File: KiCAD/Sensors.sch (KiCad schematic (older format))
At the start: 29 parts, among them U401 BME680, U402 APDS-9500, U403 LSM6DSM, U404 CMM-4030D-261-I2S-TR, U405 TSOP75340TTCT-ND, U406 MAX86150EFF+T, U407 VL6180XV0NR_1, U408 LP5907MFX-2.8

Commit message: Continue work on Schematics
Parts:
- removed U408: LP5907MFX-2.8, Package_TO_SOT_SMD:SOT-23-5, symbol Regulator_Linear:LP5907MFX-2.8
- added PW501: AP7354-18FS4, XasPrints:X2-DFN1010-4, symbol XasParts:AP7354-18FS4
- added PW502: AP7354-28FS4, XasPrints:X2-DFN1010-4, symbol XasParts:AP7354-28FS4
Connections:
- net labels removed: +1V8
- wire segments 125 -> 130
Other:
- moved on the sheet: C407, C408, C409, C410, C411, D408, R402, U403, U406

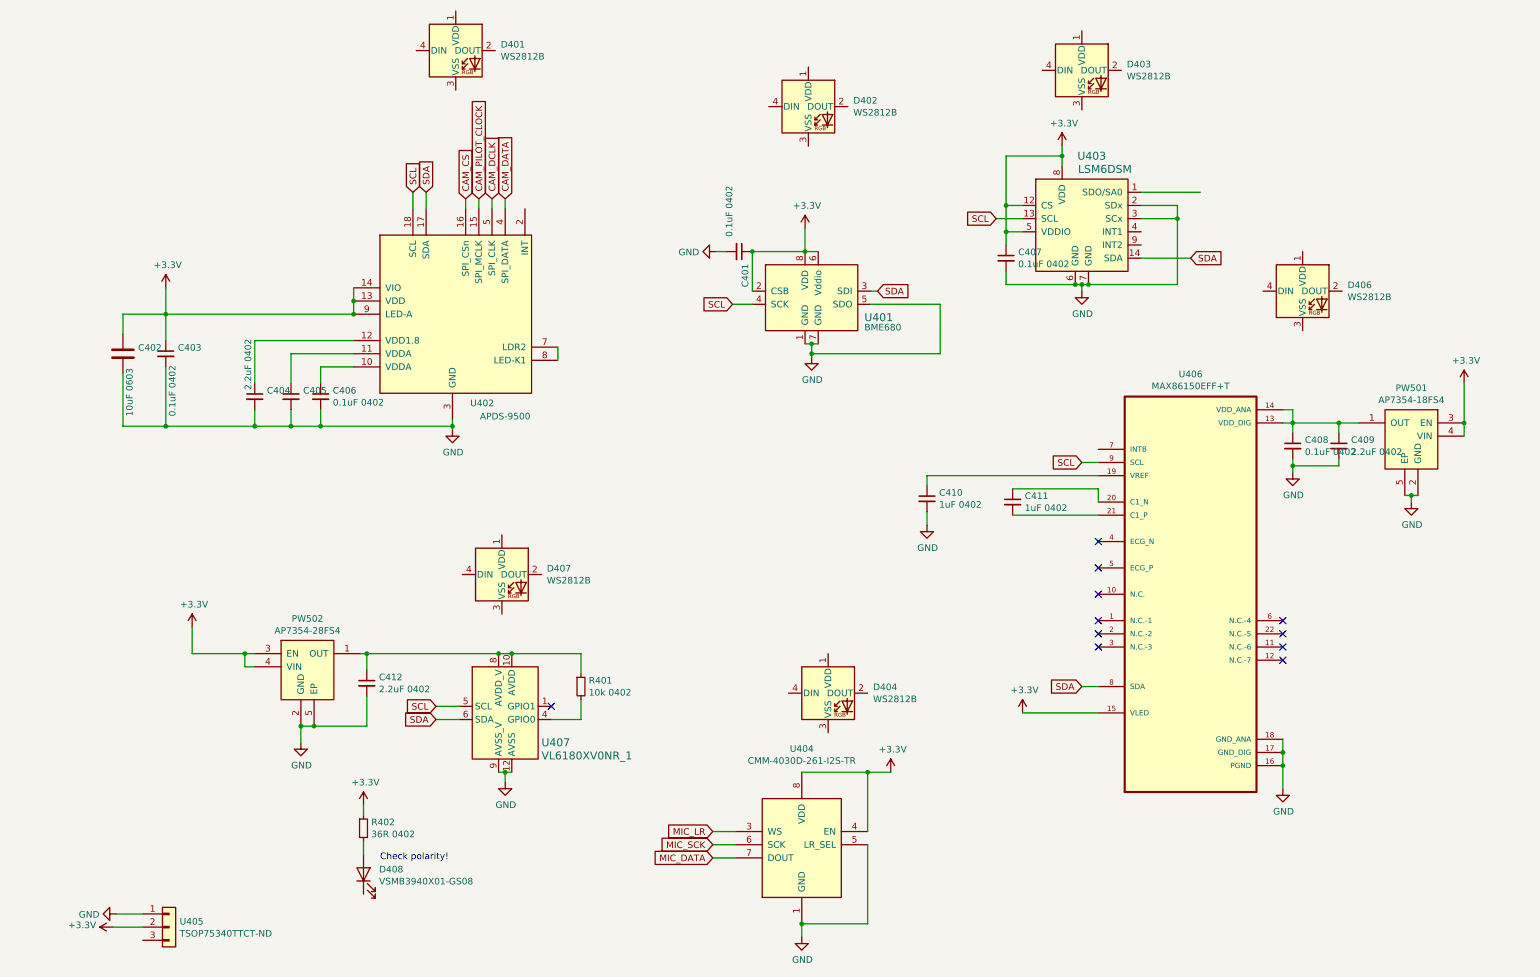
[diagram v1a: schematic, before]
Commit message: Add STM32 base circuit for power control and USB, also a lot of other things
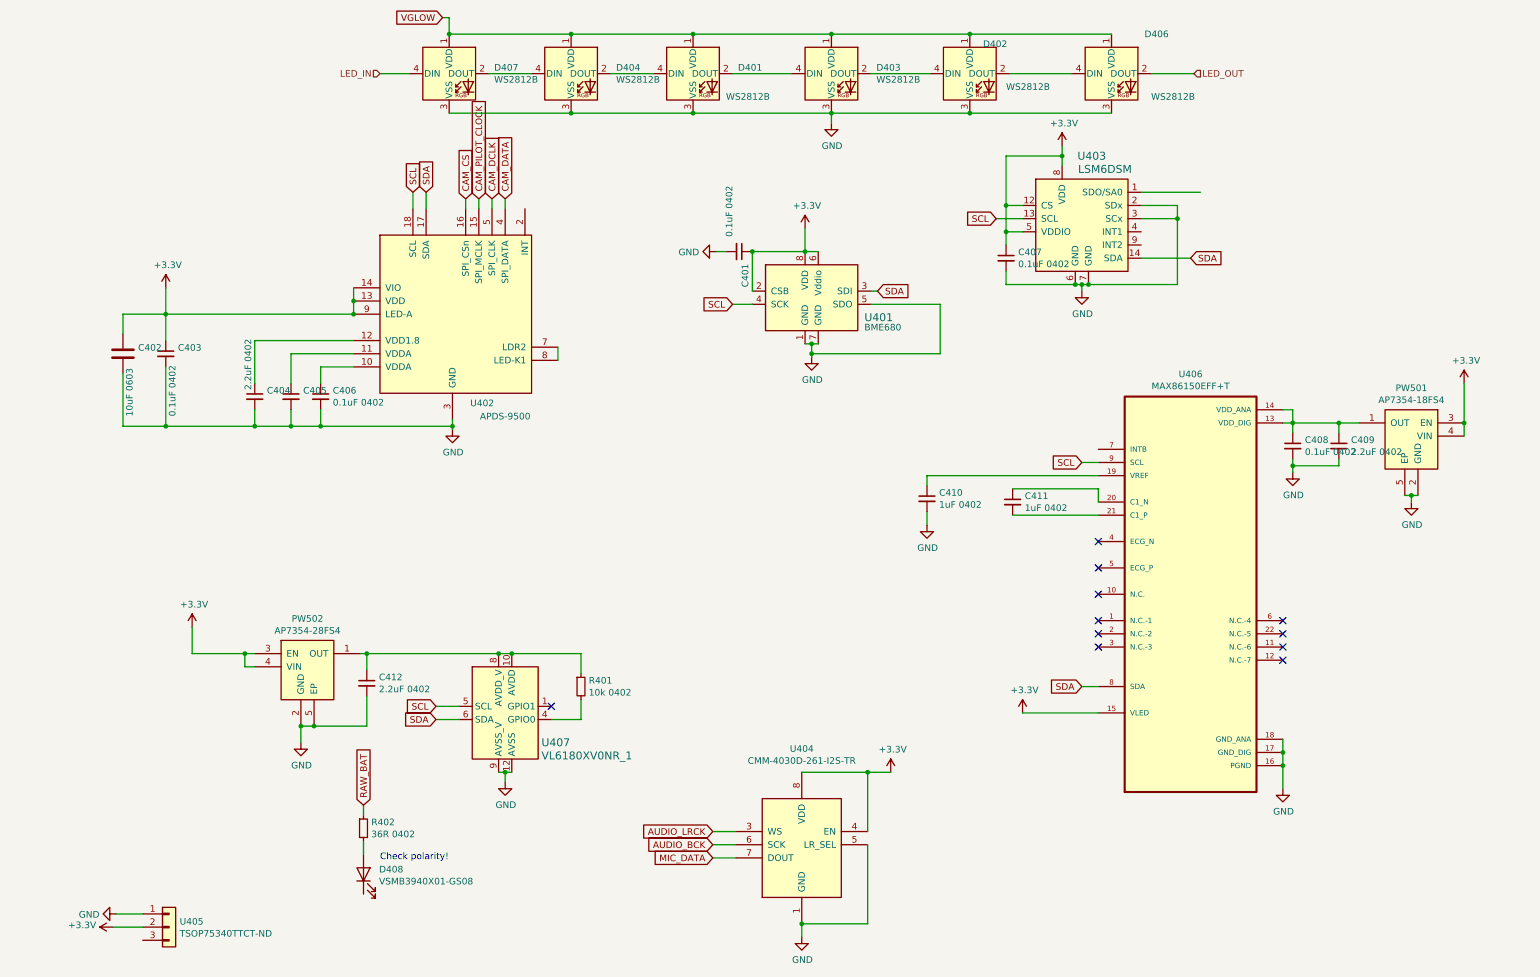
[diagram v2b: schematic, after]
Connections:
- net +3V3: no longer R402.1
- net GND: now also D401.3 (VSS), D402.3 (VSS), D403.3 (VSS), D404.3 (VSS), D406.3 (VSS), D407.3 (VSS)
- net VGLOW: now reaches D401.1 (VDD)
- net VGLOW: now also D402.1 (VDD), D403.1 (VDD), D404.1 (VDD), D406.1 (VDD), D407.1 (VDD)
- net at D401.2 (DOUT): now also D403.4 (DIN)
- net at D401.4 (DIN): now also D404.2 (DOUT)
- net at D402.2 (DOUT): now also D406.4 (DIN)
- net at D402.4 (DIN): now also D403.2 (DOUT)
- net at D404.4 (DIN): now also D407.2 (DOUT)
- net LED_OUT: now reaches D406.2 (DOUT)
- net LED_IN: now reaches D407.4 (DIN)
- net MIC_LR renamed AUDIO_LRCK
- net MIC_SCK renamed AUDIO_BCK
- new net RAW_BAT: R402.1
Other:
- moved on the sheet: D401, D402, D403, D404, D406, D407
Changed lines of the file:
@@
 $Descr A4 11693 8268
 encoding utf-8
-Sheet 5 7
+Sheet 4 6
 Title ""
 Date ""
@@
 L LED:WS2812B D401
 U 1 1 60F3BC6A
-P 3500 850
-F 0 "D401" H 3841 896 50  0000 L CNN
-F 1 "WS2812B" H 3841 805 50  0000 L CNN
-F 2 "XasPrints:SMD-LX0707RGB-TR" H 3550 550 50  0001 L TNN
-F 3 "https://cdn-shop.adafruit.com/datasheets/WS2812B.pdf" H 3600 475 50  0001 L TNN
-	1    3500 850
+P 5300 1025
+F 0 "D401" H 5641 1071 50  0000 L CNN
+F 1 "WS2812B" H 5550 850 50  0000 L CNN
+F 2 "XasPrints:SMD-LX0707RGB-TR" H 5350 725 50  0001 L TNN
+F 3 "https://cdn-shop.adafruit.com/datasheets/WS2812B.pdf" H 5400 650 50  0001 L TNN
+	1    5300 1025
 	1    0    0    -1
 $EndComp
@@
 L LED:WS2812B D402
 U 1 1 60F4C75F
-P 6175 1275
-F 0 "D402" H 6516 1321 50  0000 L CNN
-F 1 "WS2812B" H 6516 1230 50  0000 L CNN
-F 2 "XasPrints:SMD-LX0707RGB-TR" H 6225 975 50  0001 L TNN
-F 3 "https://cdn-shop.adafruit.com/datasheets/WS2812B.pdf" H 6275 900 50  0001 L TNN
-	1    6175 1275
+P 7400 1025
+F 0 "D402" H 7500 1250 50  0000 L CNN
+F 1 "WS2812B" H 7675 925 50  0000 L CNN
+F 2 "XasPrints:SMD-LX0707RGB-TR" H 7450 725 50  0001 L TNN
+F 3 "https://cdn-shop.adafruit.com/datasheets/WS2812B.pdf" H 7500 650 50  0001 L TNN
+	1    7400 1025
 	1    0    0    -1
 $EndComp
@@
 L LED:WS2812B D403
 U 1 1 60F50157
-P 8250 1000
-F 0 "D403" H 8591 1046 50  0000 L CNN
-F 1 "WS2812B" H 8591 955 50  0000 L CNN
-F 2 "XasPrints:SMD-LX0707RGB-TR" H 8300 700 50  0001 L TNN
-F 3 "https://cdn-shop.adafruit.com/datasheets/WS2812B.pdf" H 8350 625 50  0001 L TNN
-	1    8250 1000
+P 6350 1025
+F 0 "D403" H 6691 1071 50  0000 L CNN
+F 1 "WS2812B" H 6691 980 50  0000 L CNN
+F 2 "XasPrints:SMD-LX0707RGB-TR" H 6400 725 50  0001 L TNN
+F 3 "https://cdn-shop.adafruit.com/datasheets/WS2812B.pdf" H 6450 650 50  0001 L TNN
+	1    6350 1025
 	1    0    0    -1
 $EndComp
@@
 L LED:WS2812B D404
 U 1 1 60F5023D
-P 6325 5725
-F 0 "D404" H 6666 5771 50  0000 L CNN
-F 1 "WS2812B" H 6666 5680 50  0000 L CNN
-F 2 "XasPrints:SMD-LX0707RGB-TR" H 6375 5425 50  0001 L TNN
-F 3 "https://cdn-shop.adafruit.com/datasheets/WS2812B.pdf" H 6425 5350 50  0001 L TNN
-	1    6325 5725
+P 4375 1025
+F 0 "D404" H 4716 1071 50  0000 L CNN
+F 1 "WS2812B" H 4716 980 50  0000 L CNN
+F 2 "XasPrints:SMD-LX0707RGB-TR" H 4425 725 50  0001 L TNN
+F 3 "https://cdn-shop.adafruit.com/datasheets/WS2812B.pdf" H 4475 650 50  0001 L TNN
+	1    4375 1025
 	1    0    0    -1
 $EndComp
@@
 L LED:WS2812B D406
 U 1 1 60F5FA46
-P 9925 2675
-F 0 "D406" H 10266 2721 50  0000 L CNN
-F 1 "WS2812B" H 10266 2630 50  0000 L CNN
-F 2 "XasPrints:SMD-LX0707RGB-TR" H 9975 2375 50  0001 L TNN
-F 3 "https://cdn-shop.adafruit.com/datasheets/WS2812B.pdf" H 10025 2300 50  0001 L TNN
-	1    9925 2675
+P 8475 1025
+F 0 "D406" H 8725 1325 50  0000 L CNN
+F 1 "WS2812B" H 8775 850 50  0000 L CNN
+F 2 "XasPrints:SMD-LX0707RGB-TR" H 8525 725 50  0001 L TNN
+F 3 "https://cdn-shop.adafruit.com/datasheets/WS2812B.pdf" H 8575 650 50  0001 L TNN
+	1    8475 1025
 	1    0    0    -1
 $EndComp
@@
 L LED:WS2812B D407
 U 1 1 60F5FD07
-P 3850 4825
-F 0 "D407" H 4191 4871 50  0000 L CNN
-F 1 "WS2812B" H 4191 4780 50  0000 L CNN
-F 2 "XasPrints:SMD-LX0707RGB-TR" H 3900 4525 50  0001 L TNN
-F 3 "https://cdn-shop.adafruit.com/datasheets/WS2812B.pdf" H 3950 4450 50  0001 L TNN
-	1    3850 4825
+P 3450 1025
+F 0 "D407" H 3791 1071 50  0000 L CNN
+F 1 "WS2812B" H 3791 980 50  0000 L CNN
+F 2 "XasPrints:SMD-LX0707RGB-TR" H 3500 725 50  0001 L TNN
+F 3 "https://cdn-shop.adafruit.com/datasheets/WS2812B.pdf" H 3550 650 50  0001 L TNN
+	1    3450 1025
 	1    0    0    -1
 $EndComp
@@
 Connection ~ 6125 7475
 Text GLabel 5450 6775 0    50   Input ~ 0
-MIC_LR
+AUDIO_LRCK
 Text GLabel 5450 6875 0    50   Input ~ 0
-MIC_SCK
+AUDIO_BCK
 Text GLabel 5450 6975 0    50   Input ~ 0
 MIC_DATA
@@
 Wire Wire Line
 	2800 6850 2800 6950
-$Comp
-L power:+3.3V #PWR0134
-U 1 1 6105D69A
-P 2800 6575
-F 0 "#PWR0134" H 2800 6425 50  0001 C CNN
-F 1 "+3.3V" H 2815 6748 50  0000 C CNN
-F 2 "" H 2800 6575 50  0001 C CNN
-F 3 "" H 2800 6575 50  0001 C CNN
-	1    2800 6575
-	1    0    0    -1
-$EndComp
 Wire Wire Line
 	2800 6575 2800 6650
@@
 	1    0    0    -1
 $EndComp
+Wire Wire Line
+	3750 1025 4075 1025
+Wire Wire Line
+	4675 1025 5000 1025
+Wire Wire Line
+	5600 1025 6050 1025
+Wire Wire Line
+	6650 1025 7100 1025
+Wire Wire Line
+	7700 1025 8175 1025
+Wire Wire Line
+	3450 725  4375 725
+Connection ~ 4375 725
+Wire Wire Line
+	4375 725  5300 725
+Connection ~ 5300 725
+Wire Wire Line
+	5300 725  6350 725
+Connection ~ 6350 725
+Wire Wire Line
+	6350 725  7400 725
+Connection ~ 7400 725
+Wire Wire Line
+	7400 725  8475 725
+Wire Wire Line
+	8475 1325 7400 1325
+Connection ~ 4375 1325
+Wire Wire Line
+	4375 1325 3450 1325
+Connection ~ 5300 1325
+Wire Wire Line
+	5300 1325 4375 1325
+Connection ~ 6350 1325
+Wire Wire Line
+	6350 1325 5300 1325
+Connection ~ 7400 1325
+Wire Wire Line
+	7400 1325 6350 1325
+$Comp
+L power:GND #PWR0145
+U 1 1 6110EA34
+P 6350 1400
+F 0 "#PWR0145" H 6350 1150 50  0001 C CNN
+F 1 "GND" H 6355 1227 50  0000 C CNN
+F 2 "" H 6350 1400 50  0001 C CNN
+F 3 "" H 6350 1400 50  0001 C CNN
+	1    6350 1400
+	1    0    0    -1
+$EndComp
+Wire Wire Line
+	6350 1400 6350 1325
+Text GLabel 3400 600  0    50   Input ~ 0
+VGLOW
+Wire Wire Line
+	3400 600  3450 600
+Wire Wire Line
+	3450 600  3450 725
+Connection ~ 3450 725
+Text HLabel 2925 1025 0    50   Input ~ 0
+LED_IN
+Wire Wire Line
+	2925 1025 3150 1025
+Text GLabel 2800 6575 1    50   Input ~ 0
+RAW_BAT
+Text HLabel 9100 1025 2    50   Input ~ 0
+LED_OUT
+Wire Wire Line
+	9100 1025 8775 1025
 $EndSCHEMATC

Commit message: Continue work on TapV2's schematic, almost completing it!
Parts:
- added Q401: DMN3404L, Package_TO_SOT_SMD:SOT-23, symbol Transistor_FET:DMN3404L
- added R403: 36R 0402, Resistor_SMD:R_0402_1005Metric, symbol Device:R_Small
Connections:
- net GND: now also Q401.2 (S)
- net IR_RX: now reaches U405.3 (Pin_3)
- net at D408.1 (K): now also Q401.3 (D)
- new net: Q401.1 (G), R403.1
- new net IR_TX: R403.2
- no-connect marks 11 -> 12
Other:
- moved on the sheet: C402, C403, C404, C405, C406, D408, R402, U402

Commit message: Finalize PCB schematics
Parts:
- added C413, C414: 0.1uF 0402, Capacitor_SMD:C_0402_1005Metric, symbol Device:C_Small
- added R404: 100R 0402, Resistor_SMD:R_0402_1005Metric, symbol Device:R_Small
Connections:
- net +3V3: now also R404.2; no longer U405.2 (Pin_2)
- net GND: now also U403.1 (SDO/SA0), C413.1, C414.1
- net VGLOW: now also C413.2
- net KNOCK_INT: now reaches U402.2 (INT)
- net KNOCK_INT: now also U403.4 (INT1)
- new net: C414.2, R404.1, U405.2 (Pin_2)
- no-connect marks 12 -> 13
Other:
- note added: "7bit addr: 0x29"
- note added: "7bit addr: 0x5E"
- note added: "7bit addr: 0x6A"
- note added: "7bit addr: 0x73\n"
- note added: "7bit addr: 0x76"
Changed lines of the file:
@@
 $EndComp
 Wire Wire Line
-	925  7400 1125 7400
+	925  7400 1000 7400
 $Comp
 L power:+3.3V #PWR0133
 U 1 1 61032906
-P 900 7500
-F 0 "#PWR0133" H 900 7350 50  0001 C CNN
-F 1 "+3.3V" V 915 7628 50  0000 L CNN
-F 2 "" H 900 7500 50  0001 C CNN
-F 3 "" H 900 7500 50  0001 C CNN
-	1    900  7500
-	0    -1   -1   0
-$EndComp
-Wire Wire Line
-	900  7500 1125 7500
+P 650 7125
+F 0 "#PWR0133" H 650 6975 50  0001 C CNN
+F 1 "+3.3V" V 665 7253 50  0000 L CNN
+F 2 "" H 650 7125 50  0001 C CNN
+F 3 "" H 650 7125 50  0001 C CNN
+	1    650  7125
+	1    0    0    -1
+$EndComp
 $Comp
 L Device:C_Small C?
@@
 Connection ~ 5300 725
 Wire Wire Line
-	5300 725  6350 725
+	5300 725  5925 725
 Connection ~ 6350 725
 Wire Wire Line
@@
 Text GLabel 775  6775 0    50   Input ~ 0
 IR_TX
-Wire Notes Line
-	8850 1600 8850 2125
-Wire Notes Line
-	8850 2125 9325 2125
-Wire Notes Line
-	9325 2125 9325 1600
-Wire Notes Line
-	9325 1600 8850 1600
+$Comp
+L power:GND #PWR0160
+U 1 1 61445520
+P 9150 1925
+F 0 "#PWR0160" H 9150 1675 50  0001 C CNN
+F 1 "GND" H 9155 1752 50  0000 C CNN
+F 2 "" H 9150 1925 50  0001 C CNN
+F 3 "" H 9150 1925 50  0001 C CNN
+	1    9150 1925
+	1    0    0    -1
+$EndComp
+Text Notes 6525 3300 0    50   ~ 0
+7bit addr: 0x76
+Text Notes 8650 2750 0    50   ~ 0
+7bit addr: 0x6A
+Text Notes 3825 4050 0    50   ~ 0
+7bit addr: 0x73\n
+Text Notes 3600 5375 0    50   ~ 0
+7bit addr: 0x29
+Text Notes 10100 4725 0    50   ~ 0
+7bit addr: 0x5E
+NoConn ~ 8700 2325
+Text GLabel 9075 2225 2    50   Input ~ 0
+KNOCK_INT
+Wire Wire Line
+	8700 2225 9075 2225
+$Comp
+L Device:C_Small C?
+U 1 1 61441ACA
+P 5925 825
+AR Path="/60EDF44C/61441ACA" Ref="C?"  Part="1"
+AR Path="/60F2BC2A/61441ACA" Ref="C413"  Part="1"
+F 0 "C413" H 6017 871 50  0000 L CNN
+F 1 "0.1uF 0402" H 5425 750 50  0000 L CNN
+F 2 "Capacitor_SMD:C_0402_1005Metric" H 5925 825 50  0001 C CNN
+F 3 "~" H 5925 825 50  0001 C CNN
+	1    5925 825
+	-1   0    0    1
+$EndComp
+Connection ~ 5925 725
+Wire Wire Line
+	5925 725  6350 725
+$Comp
+L power:GND #PWR0164
+U 1 1 61441DD6
+P 5925 1400
+F 0 "#PWR0164" H 5925 1150 50  0001 C CNN
+F 1 "GND" H 5930 1227 50  0000 C CNN
+F 2 "" H 5925 1400 50  0001 C CNN
+F 3 "" H 5925 1400 50  0001 C CNN
+	1    5925 1400
+	1    0    0    -1
+$EndComp
+Wire Wire Line
+	5925 1400 5925 925
+Text GLabel 4150 2175 2    50   Input ~ 0
+KNOCK_INT
+Wire Wire Line
+	4025 2300 4025 2175
+Wire Wire Line
+	4025 2175 4150 2175
+$Comp
+L Device:R_Small R404
+U 1 1 614BAC36
+P 650 7225
+F 0 "R404" H 709 7271 50  0000 L CNN
+F 1 "100R 0402" H 709 7180 50  0000 L CNN
+F 2 "Resistor_SMD:R_0402_1005Metric" H 650 7225 50  0001 C CNN
+F 3 "~" H 650 7225 50  0001 C CNN
+	1    650  7225
+	-1   0    0    1
+$EndComp
+$Comp
+L Device:C_Small C?
+U 1 1 614BCC79
+P 800 7225
+AR Path="/60EDF44C/614BCC79" Ref="C?"  Part="1"
+AR Path="/60F2BC2A/614BCC79" Ref="C414"  Part="1"
+F 0 "C414" H 892 7271 50  0000 L CNN
+F 1 "0.1uF 0402" H 300 7150 50  0000 L CNN
+F 2 "Capacitor_SMD:C_0402_1005Metric" H 800 7225 50  0001 C CNN
+F 3 "~" H 800 7225 50  0001 C CNN
+	1    800  7225
+	1    0    0    -1
+$EndComp
+Wire Wire Line
+	650  7325 800  7325
+Wire Wire Line
+	800  7125 1000 7125
+Wire Wire Line
+	1000 7125 1000 7400
+Connection ~ 1000 7400
+Wire Wire Line
+	1000 7400 1125 7400
+Wire Wire Line
+	650  7325 650  7500
+Wire Wire Line
+	650  7500 1125 7500
+Connection ~ 650  7325
 $EndSCHEMATC
